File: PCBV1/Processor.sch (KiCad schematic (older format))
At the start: 1 part

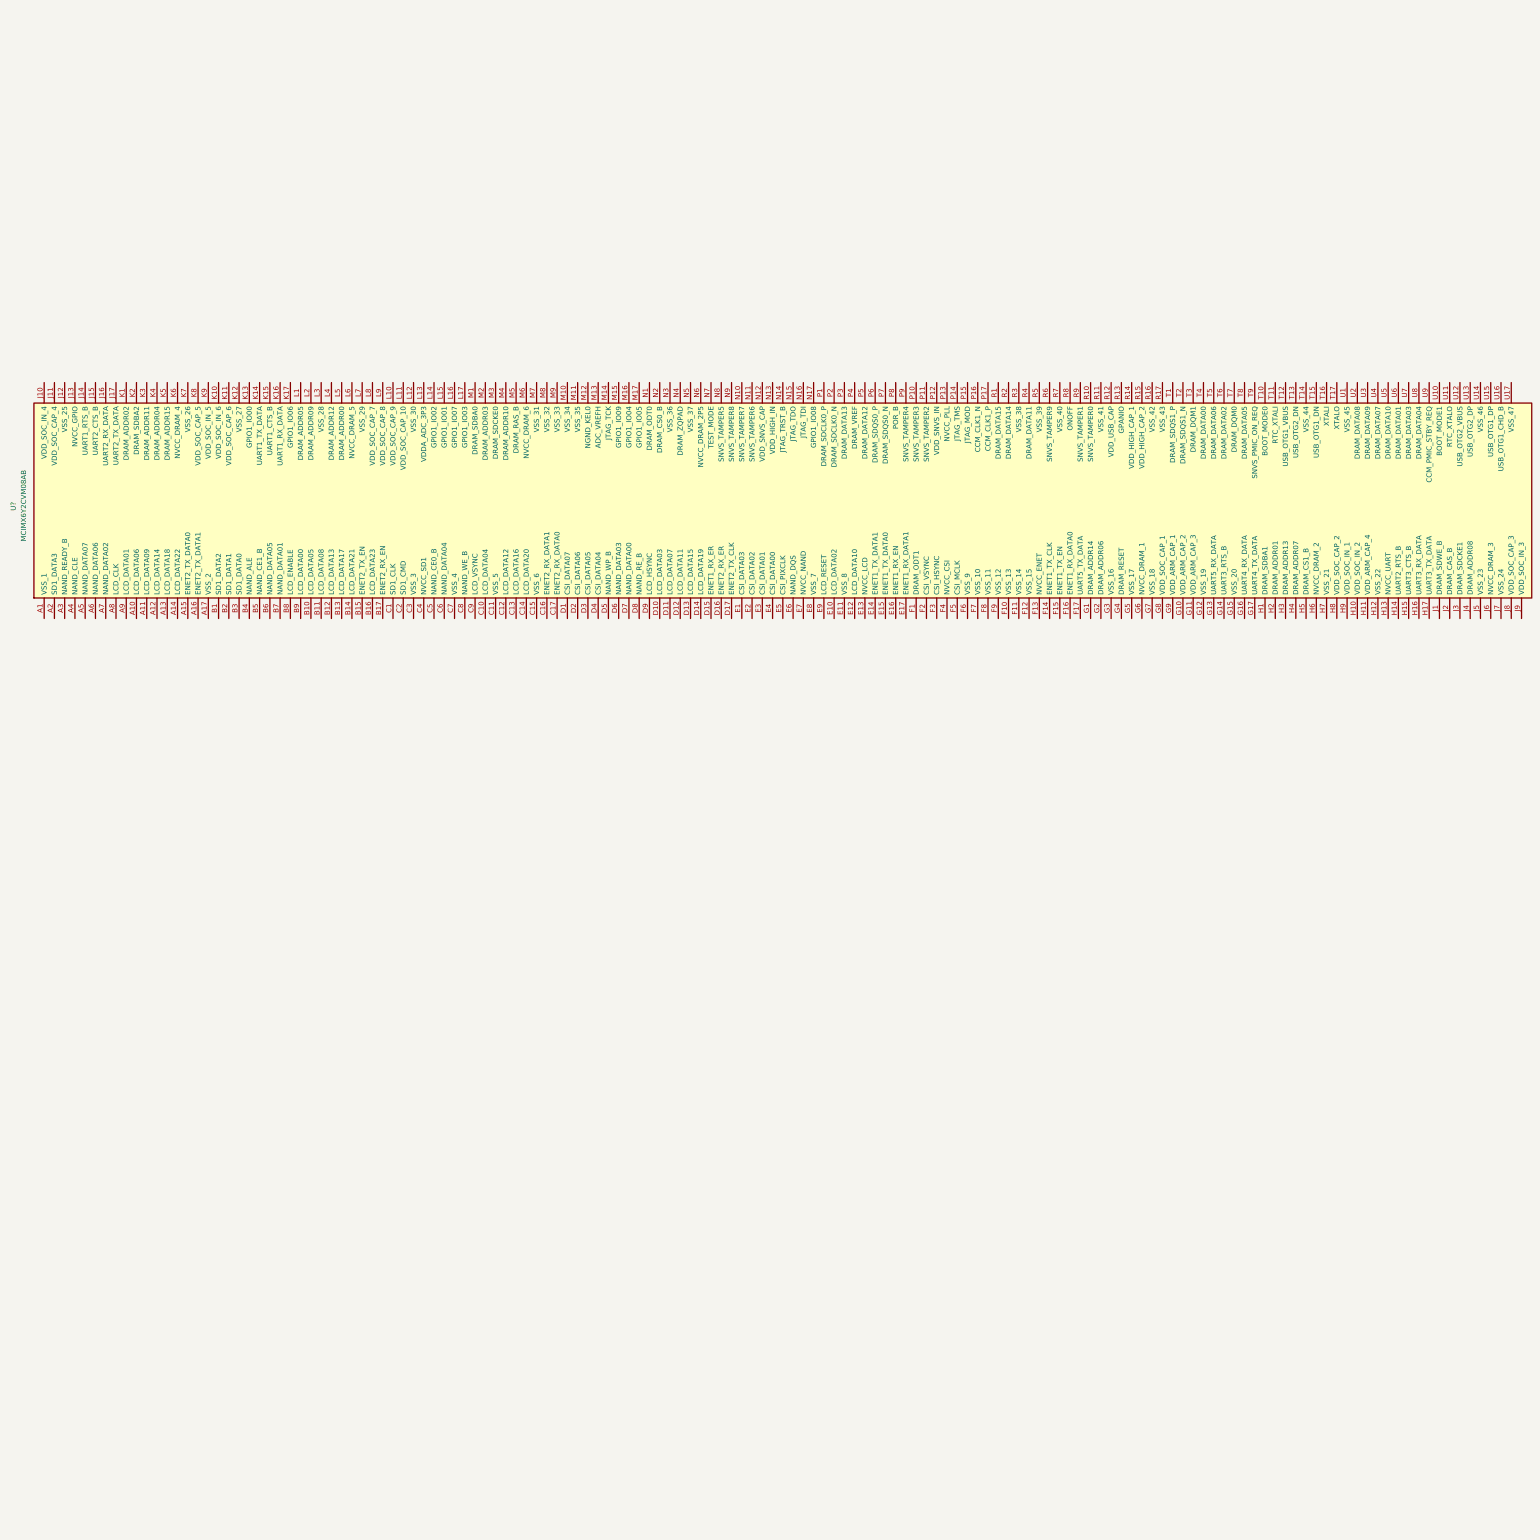
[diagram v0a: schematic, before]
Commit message: Added schematic for power through barrel jack and voltage converters, connected DRAM.
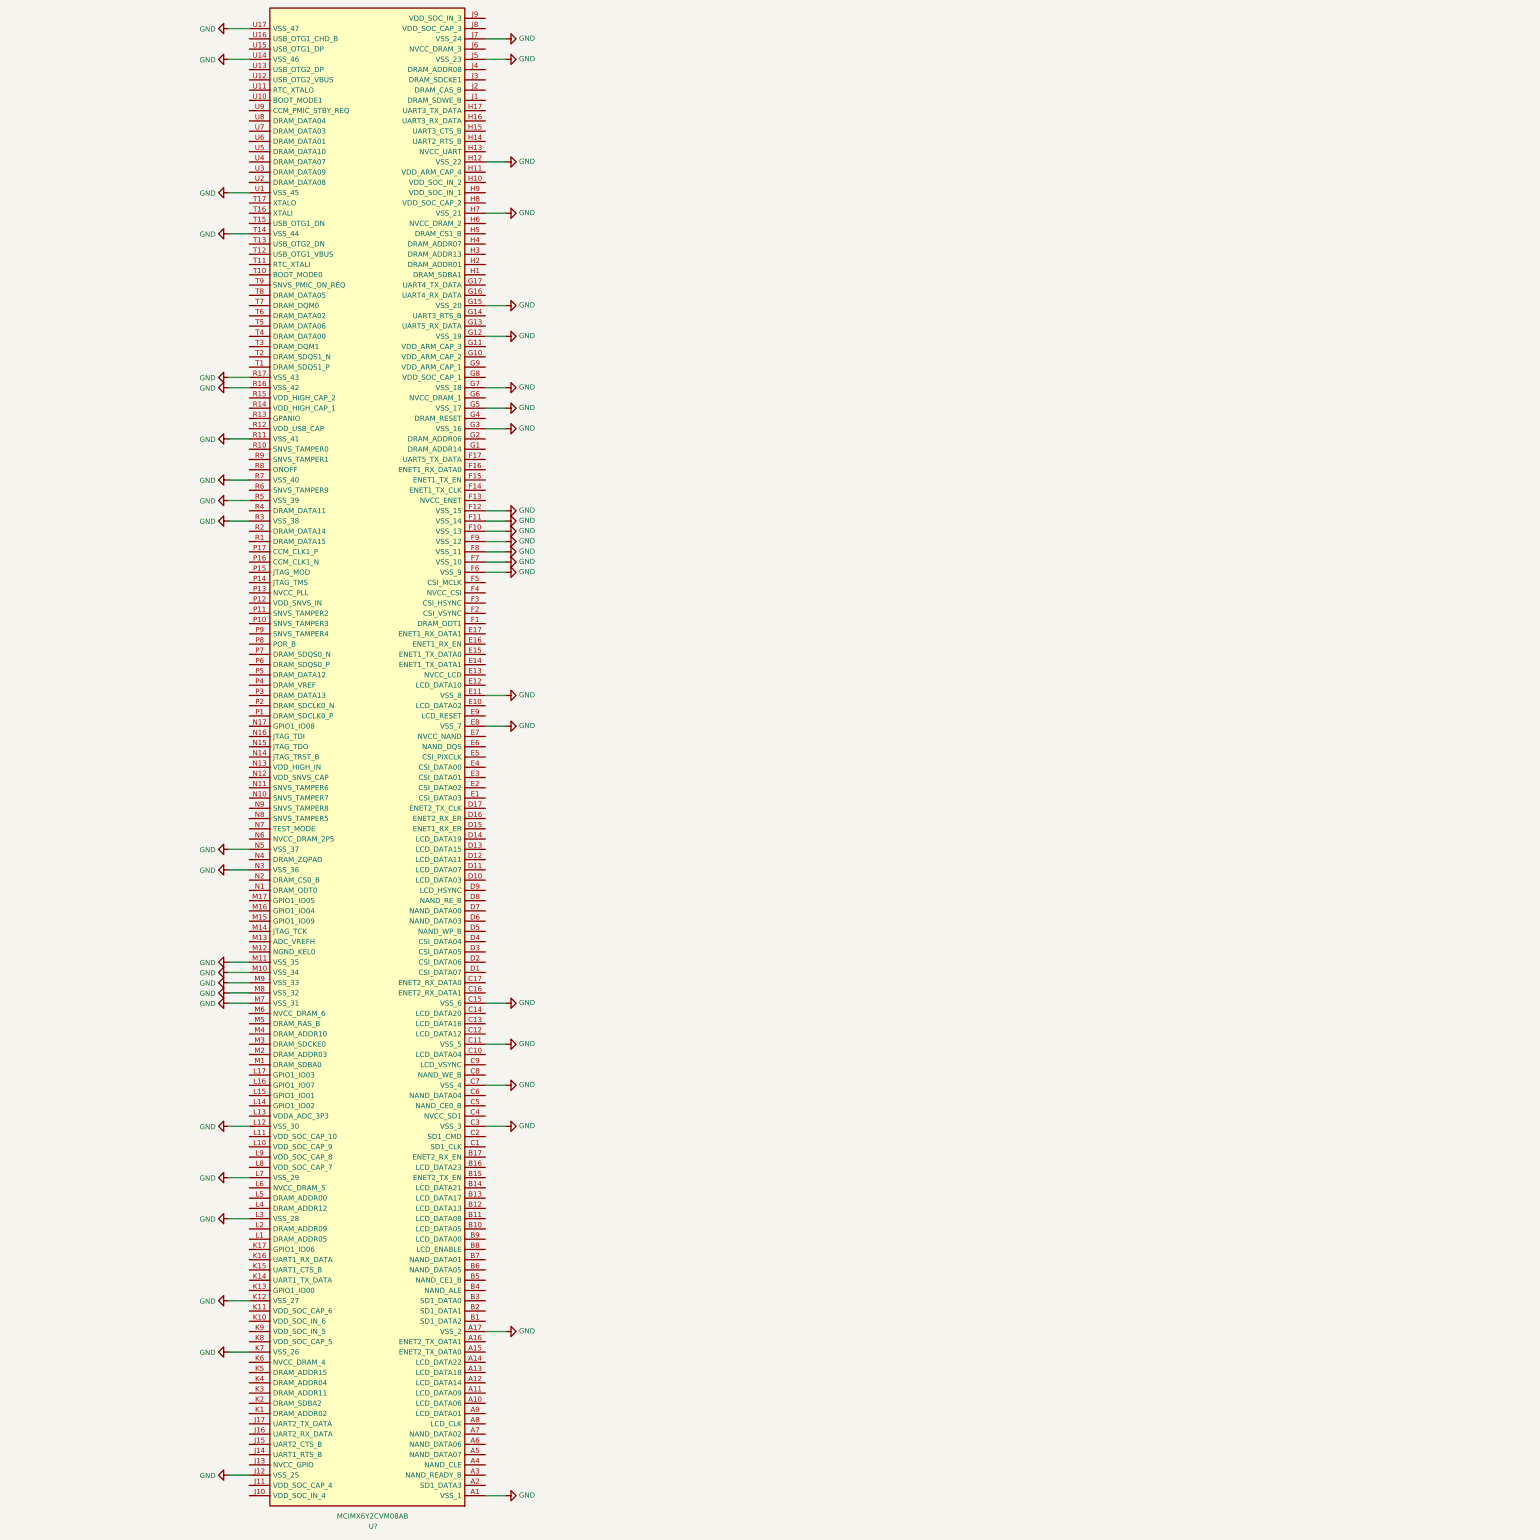
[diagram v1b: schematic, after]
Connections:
- net GND: now reaches U?.A1 (VSS_1)
- net GND: now also U?.A17 (VSS_2), U?.C11 (VSS_5), U?.C15 (VSS_6), U?.C3 (VSS_3), U?.C7 (VSS_4), U?.E11 (VSS_8), U?.E8 (VSS_7), U?.F10 (VSS_13), U?.F11 (VSS_14), U?.F12 (VSS_15), U?.F6 (VSS_9), U?.F7 (VSS_10), U?.F8 (VSS_11), U?.F9 (VSS_12), U?.G12 (VSS_19), U?.G15 (VSS_20), U?.G3 (VSS_16), U?.G5 (VSS_17), U?.G7 (VSS_18), U?.H12 (VSS_22), U?.H7 (VSS_21), U?.J12 (VSS_25), U?.J5 (VSS_23), U?.J7 (VSS_24), U?.K12 (VSS_27), U?.K7 (VSS_26), U?.L12 (VSS_30), U?.L3 (VSS_28), U?.L7 (VSS_29), U?.M10 (VSS_34), U?.M11 (VSS_35), U?.M7 (VSS_31), U?.M8 (VSS_32), U?.M9 (VSS_33), U?.N3 (VSS_36), U?.N5 (VSS_37), U?.R11 (VSS_41), U?.R16 (VSS_42), U?.R17 (VSS_43), U?.R3 (VSS_38), U?.R5 (VSS_39), U?.R7 (VSS_40), U?.T14 (VSS_44), U?.U1 (VSS_45), U?.U14 (VSS_46), U?.U17 (VSS_47)
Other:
- moved on the sheet: U?

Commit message: Changes to DDR schematic.
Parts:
- added R?: 240R, symbol Device:R
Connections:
- net GND: now also R?.1
- net at U?.N4 (DRAM_ZQPAD): now also R?.2
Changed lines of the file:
@@
 Wire Wire Line
 	5550 1150 5350 1150
+$Comp
+L Device:R R?
+U 1 1 60329A40
+P 2700 9150
+F 0 "R?" V 2700 9350 50  0000 C CNN
+F 1 "240R" V 2700 9150 50  0000 C CNN
+F 2 "" V 2630 9150 50  0001 C CNN
+F 3 "~" H 2700 9150 50  0001 C CNN
+	1    2700 9150
+	0    -1   -1   0
+$EndComp
+Wire Wire Line
+	2550 9150 2350 9150
+$Comp
+L power:GND #PWR?
+U 1 1 60329A47
+P 2350 9150
+F 0 "#PWR?" H 2350 8900 50  0001 C CNN
+F 1 "GND" V 2355 9022 50  0000 R CNN
+F 2 "" H 2350 9150 50  0001 C CNN
+F 3 "" H 2350 9150 50  0001 C CNN
+	1    2350 9150
+	0    1    1    0
+$EndComp
+Wire Wire Line
+	3050 9150 2850 9150
 $EndSCHEMATC

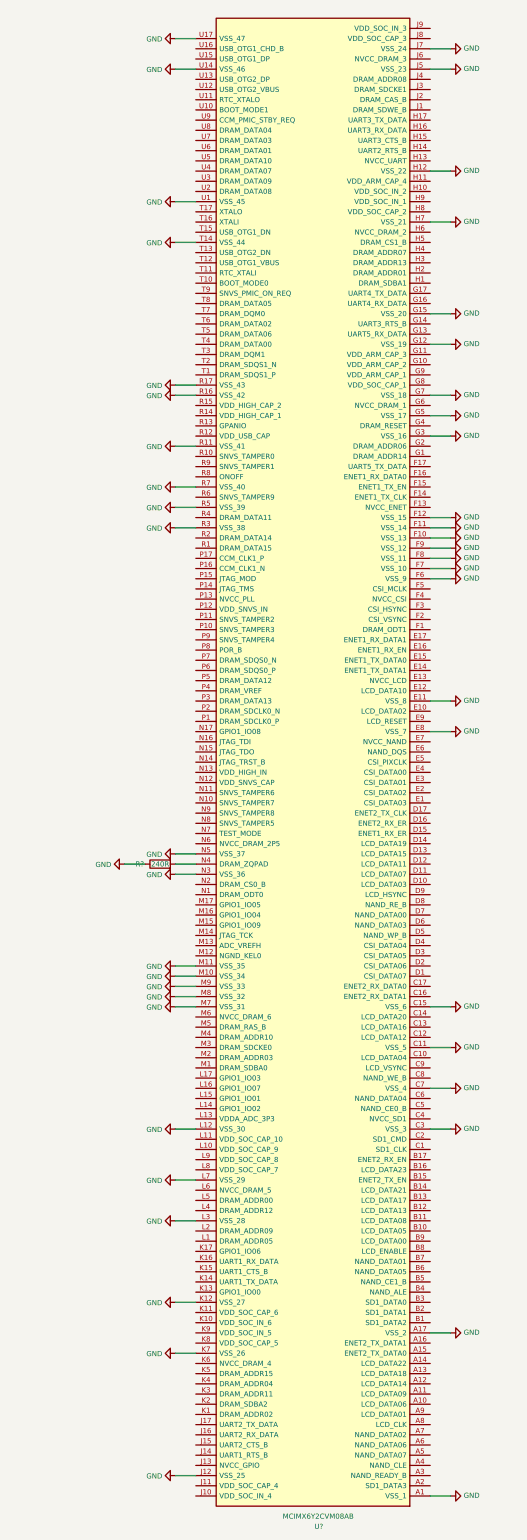
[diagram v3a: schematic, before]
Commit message: Merge of recent changes to default master (#2)
* Made a bunch of very small changes.

* Added UART, modifications to video etc.

* Minor adjustments with video connections.

* Finished video signals, added HDMI and SD connectors.
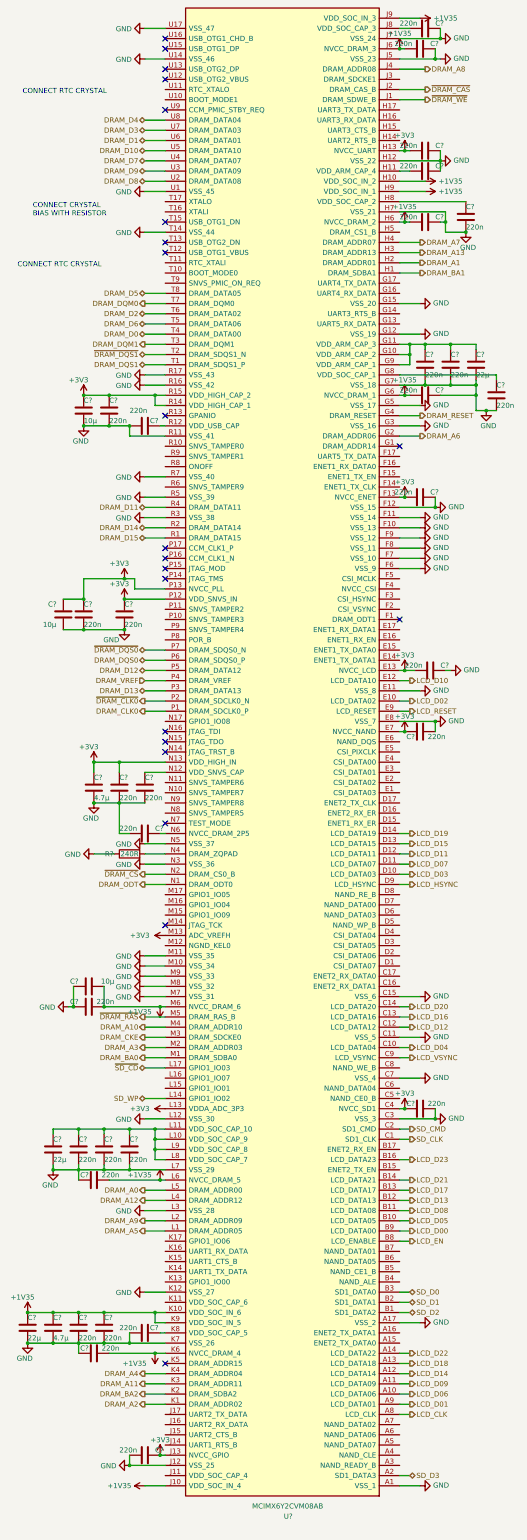
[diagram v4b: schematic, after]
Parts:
- added C? (x3): 22µ, symbol Device:C
- added C? (x2): 4.7µ, symbol Device:C
- added C? (x31): 220n, symbol Device:C
- added C? (x3): 10µ, symbol Device:C
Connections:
- net GND: now also C?.1, C?.1, C?.1, C?.1, C?.1, C?.1, C?.1, C?.1, C?.1, C?.1, C?.1, C?.1, C?.2, C?.2, C?.2, C?.2, C?.2, C?.2, C?.2, C?.2, C?.2, C?.2, C?.2, C?.2, C?.2, C?.2, C?.2, C?.2, C?.2, C?.2, C?.2, C?.2, C?.2, C?.2, C?.2, C?.2, C?.2, C?.2, C?.2
- net LCD_D06: now reaches U?.A10 (LCD_DATA06)
- net LCD_D09: now reaches U?.A11 (LCD_DATA09)
- net LCD_D14: now reaches U?.A12 (LCD_DATA14)
- net LCD_D18: now reaches U?.A13 (LCD_DATA18)
- net LCD_D22: now reaches U?.A14 (LCD_DATA22)
- net SD_D3: now reaches U?.A2 (SD1_DATA3)
- net LCD_CLK: now reaches U?.A8 (LCD_CLK)
- net LCD_D01: now reaches U?.A9 (LCD_DATA01)
- net SD_D2: now reaches U?.B1 (SD1_DATA2)
- net LCD_D05: now reaches U?.B10 (LCD_DATA05)
- net LCD_D08: now reaches U?.B11 (LCD_DATA08)
- net LCD_D13: now reaches U?.B12 (LCD_DATA13)
- net LCD_D17: now reaches U?.B13 (LCD_DATA17)
- net LCD_D21: now reaches U?.B14 (LCD_DATA21)
- net LCD_D23: now reaches U?.B16 (LCD_DATA23)
- net SD_D1: now reaches U?.B2 (SD1_DATA1)
- net SD_D0: now reaches U?.B3 (SD1_DATA0)
- net LCD_EN: now reaches U?.B8 (LCD_ENABLE)
- net LCD_D00: now reaches U?.B9 (LCD_DATA00)
- net SD_CLK: now reaches U?.C1 (SD1_CLK)
- net LCD_D04: now reaches U?.C10 (LCD_DATA04)
- net LCD_D12: now reaches U?.C12 (LCD_DATA12)
- net LCD_D16: now reaches U?.C13 (LCD_DATA16)
- net LCD_D20: now reaches U?.C14 (LCD_DATA20)
- net SD_CMD: now reaches U?.C2 (SD1_CMD)
- net +3V3: now reaches U?.C4 (NVCC_SD1)
- net +3V3: now also U?.E13 (NVCC_LCD), U?.E7 (NVCC_NAND), U?.F13 (NVCC_ENET), U?.H13 (NVCC_UART), U?.J13 (NVCC_GPIO), U?.L13 (VDDA_ADC_3P3), U?.M13 (ADC_VREFH), U?.N13 (VDD_HIGH_IN), U?.P12 (VDD_SNVS_IN), U?.P13 (NVCC_PLL), U?.R14 (VDD_HIGH_CAP_1), U?.R15 (VDD_HIGH_CAP_2), C?.1, C?.1, C?.1, C?.1, C?.1, C?.1, C?.1, C?.1, C?.1, C?.1, C?.2, C?.2, C?.2
- net LCD_VSYNC: now reaches U?.C9 (LCD_VSYNC)
- net LCD_D03: now reaches U?.D10 (LCD_DATA03)
- net LCD_D07: now reaches U?.D11 (LCD_DATA07)
- net LCD_D11: now reaches U?.D12 (LCD_DATA11)
- net LCD_D15: now reaches U?.D13 (LCD_DATA15)
- net LCD_D19: now reaches U?.D14 (LCD_DATA19)
- net LCD_HSYNC: now reaches U?.D9 (LCD_HSYNC)
- net LCD_D02: now reaches U?.E10 (LCD_DATA02)
- net LCD_D10: now reaches U?.E12 (LCD_DATA10)
- net LCD_RESET: now reaches U?.E9 (LCD_RESET)
- net at U?.G10 (VDD_ARM_CAP_2): now also U?.G11 (VDD_ARM_CAP_3), U?.G9 (VDD_ARM_CAP_1), C?.1, C?.1, C?.1
- net DRAM_A6: now reaches U?.G2 (DRAM_ADDR06)
- net DRAM_RESET: now reaches U?.G4 (DRAM_RESET)
- net +1V35: now reaches U?.G6 (NVCC_DRAM_1)
- net +1V35: now also U?.H10 (VDD_SOC_IN_2), U?.H6 (NVCC_DRAM_2), U?.H9 (VDD_SOC_IN_1), U?.J10 (VDD_SOC_IN_4), U?.J6 (NVCC_DRAM_3), U?.J9 (VDD_SOC_IN_3), U?.K10 (VDD_SOC_IN_6), U?.K6 (NVCC_DRAM_4), U?.K9 (VDD_SOC_IN_5), U?.L6 (NVCC_DRAM_5), U?.M6 (NVCC_DRAM_6), C?.1, C?.1, C?.1, C?.1, C?.2, C?.2, C?.2, C?.2, C?.2, C?.2, C?.2
- net at U?.G8 (VDD_SOC_CAP_1): now also C?.1
- net DRAM_BA1: now reaches U?.H1 (DRAM_SDBA1)
- net at U?.H11 (VDD_ARM_CAP_4): now also C?.2
- net DRAM_A1: now reaches U?.H2 (DRAM_ADDR01)
- net DRAM_A13: now reaches U?.H3 (DRAM_ADDR13)
- net DRAM_A7: now reaches U?.H4 (DRAM_ADDR07)
- net at U?.H8 (VDD_SOC_CAP_2): now also C?.1
- net ~DRAM_WE: now reaches U?.J1 (DRAM_SDWE_B)
- net ~DRAM_CAS: now reaches U?.J2 (DRAM_CAS_B)
- net DRAM_A8: now reaches U?.J4 (DRAM_ADDR08)
- net at U?.J8 (VDD_SOC_CAP_3): now also C?.2
- net DRAM_A2: now reaches U?.K1 (DRAM_ADDR02)
- net DRAM_BA2: now reaches U?.K2 (DRAM_SDBA2)
- net DRAM_A11: now reaches U?.K3 (DRAM_ADDR11)
- net DRAM_A4: now reaches U?.K4 (DRAM_ADDR04)
- net at U?.K8 (VDD_SOC_CAP_5): now also C?.1
- net DRAM_A5: now reaches U?.L1 (DRAM_ADDR05)
- net at U?.L10 (VDD_SOC_CAP_9): now also U?.L11 (VDD_SOC_CAP_10), U?.L8 (VDD_SOC_CAP_7), U?.L9 (VDD_SOC_CAP_8), C?.1, C?.1, C?.1, C?.1
- net SD_WP: now reaches U?.L14 (GPIO1_IO02)
- net ~SD_CD: now reaches U?.L17 (GPIO1_IO03)
- net DRAM_A9: now reaches U?.L2 (DRAM_ADDR09)
- net DRAM_A12: now reaches U?.L4 (DRAM_ADDR12)
- net DRAM_A0: now reaches U?.L5 (DRAM_ADDR00)
- net DRAM_BA0: now reaches U?.M1 (DRAM_SDBA0)
- net DRAM_A3: now reaches U?.M2 (DRAM_ADDR03)
- net DRAM_CKE: now reaches U?.M3 (DRAM_SDCKE0)
- net DRAM_A10: now reaches U?.M4 (DRAM_ADDR10)
- net ~DRAM_RAS: now reaches U?.M5 (DRAM_RAS_B)
- net DRAM_ODT: now reaches U?.N1 (DRAM_ODT0)
- net at U?.N12 (VDD_SNVS_CAP): now also C?.1
- net ~DRAM_CS: now reaches U?.N2 (DRAM_CS0_B)
- net at U?.N6 (NVCC_DRAM_2P5): now also C?.1
- net DRAM_CLK0: now reaches U?.P1 (DRAM_SDCLK0_P)
- net ~DRAM_CLK0: now reaches U?.P2 (DRAM_SDCLK0_N)
- net DRAM_D13: now reaches U?.P3 (DRAM_DATA13)
- net DRAM_VREF: now reaches U?.P4 (DRAM_VREF)
- net DRAM_D12: now reaches U?.P5 (DRAM_DATA12)
- net DRAM_DQS0: now reaches U?.P6 (DRAM_SDQS0_P)
- net ~DRAM_DQS0: now reaches U?.P7 (DRAM_SDQS0_N)
- net DRAM_D15: now reaches U?.R1 (DRAM_DATA15)
- net at U?.R12 (VDD_USB_CAP): now also C?.1
- net DRAM_D14: now reaches U?.R2 (DRAM_DATA14)
- net DRAM_D11: now reaches U?.R4 (DRAM_DATA11)
- net DRAM_DQS1: now reaches U?.T1 (DRAM_SDQS1_P)
- net ~DRAM_DQS1: now reaches U?.T2 (DRAM_SDQS1_N)
- net DRAM_DQM1: now reaches U?.T3 (DRAM_DQM1)
- net DRAM_D0: now reaches U?.T4 (DRAM_DATA00)
- net DRAM_D6: now reaches U?.T5 (DRAM_DATA06)
- net DRAM_D2: now reaches U?.T6 (DRAM_DATA02)
- net DRAM_DQM0: now reaches U?.T7 (DRAM_DQM0)
- net DRAM_D5: now reaches U?.T8 (DRAM_DATA05)
- net DRAM_D8: now reaches U?.U2 (DRAM_DATA08)
- net DRAM_D9: now reaches U?.U3 (DRAM_DATA09)
- net DRAM_D7: now reaches U?.U4 (DRAM_DATA07)
- net DRAM_D10: now reaches U?.U5 (DRAM_DATA10)
- net DRAM_D1: now reaches U?.U6 (DRAM_DATA01)
- net DRAM_D3: now reaches U?.U7 (DRAM_DATA03)
- net DRAM_D4: now reaches U?.U8 (DRAM_DATA04)
- no-connect marks 0 -> 21
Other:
- note added: "CONNECT CRYSTAL\nBIAS WITH RESISTOR"
- note added: "CONNECT RTC CRYSTAL"
- moved on the sheet: R?, U?
